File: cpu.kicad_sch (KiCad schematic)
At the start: 29 parts, among them J1 USB_C_Receptacle, SW1 TL3342F160QG/TR, SW2 TL3342F160QG/TR, U4 RP2040, U5 LM4040DBZ-3, U6 W25Q32JVSS, Y1 Crystal

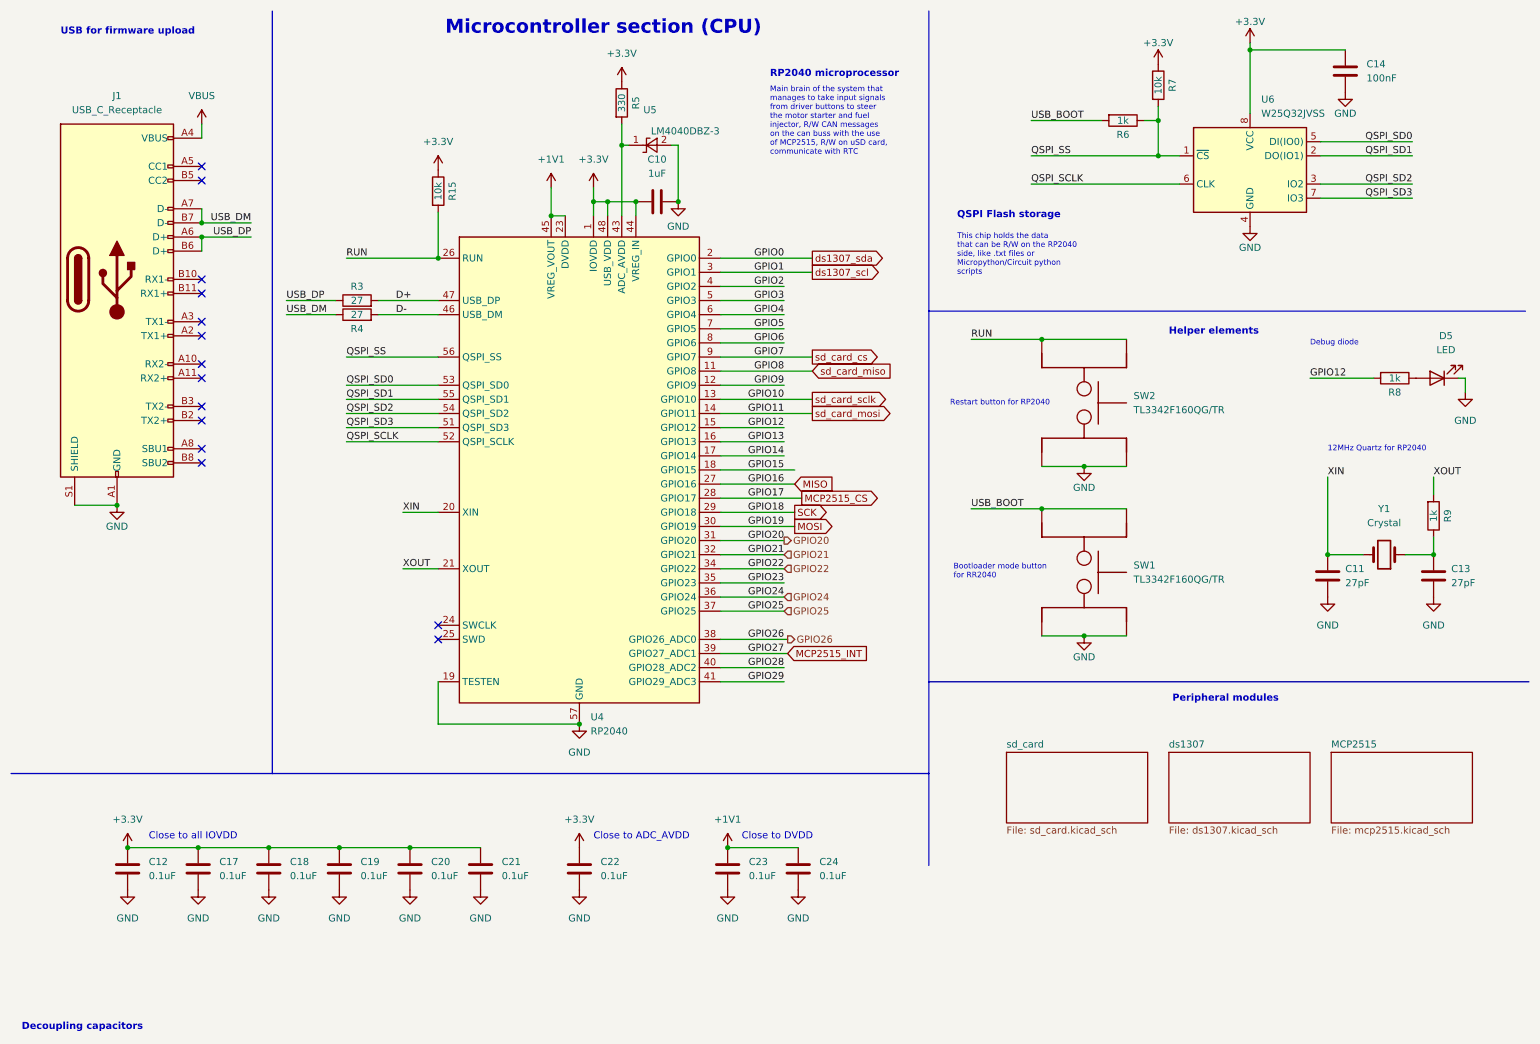
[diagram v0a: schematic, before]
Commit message: Added 12V regulator for injector
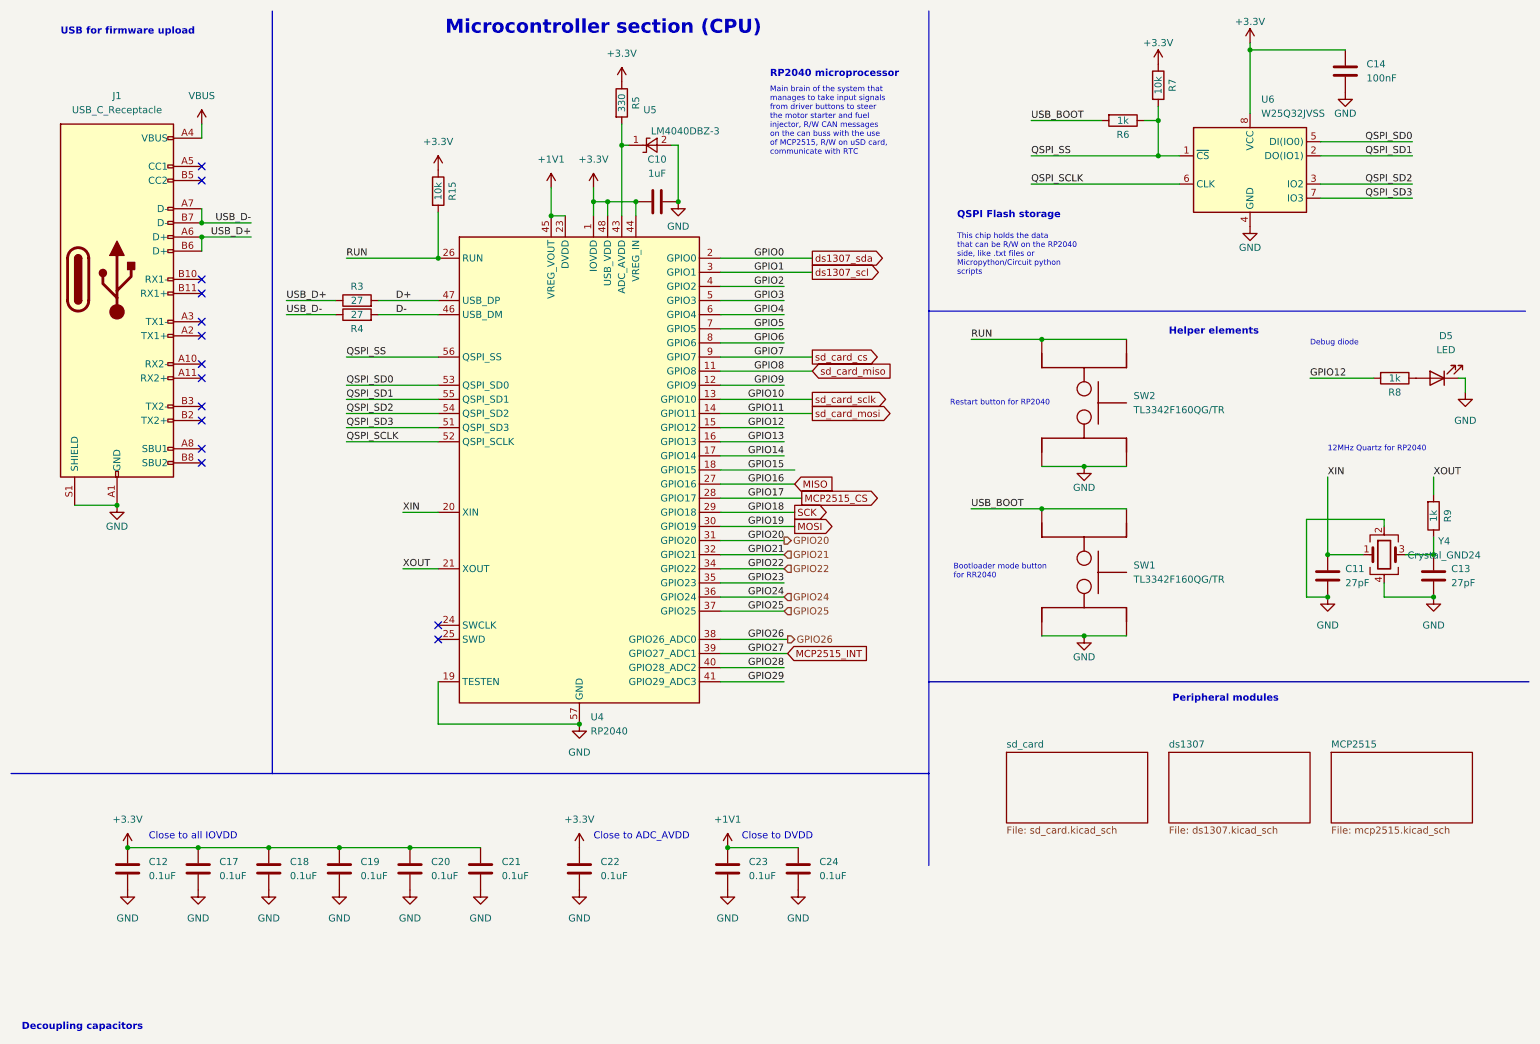
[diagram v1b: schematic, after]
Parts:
- removed Y1: Crystal, Crystal:Crystal_SMD_3225-4Pin_3.2x2.5mm, symbol Device:Crystal
- added Y4: Crystal_GND24, symbol Device:Crystal_GND24
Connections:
- net GND: now also Y4.2, Y4.4
- net XIN: now also Y4.1
- net at C13.1, R9.1: now also Y4.3
- net USB_DM renamed USB_D-
- net USB_DP renamed USB_D+
